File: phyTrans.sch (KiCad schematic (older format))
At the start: 2 parts

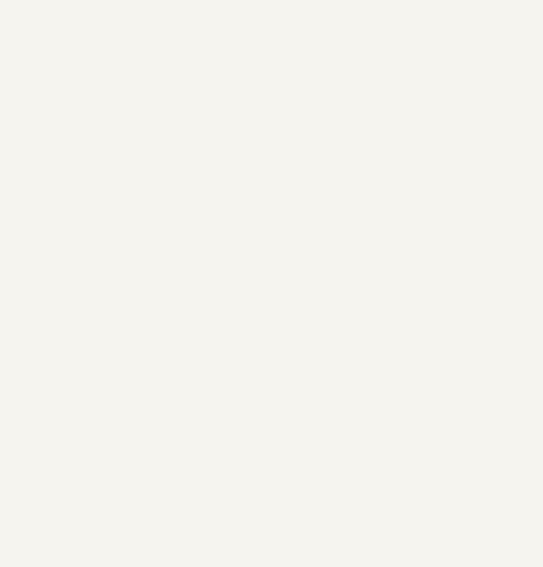
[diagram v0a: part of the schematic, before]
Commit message: Added user fields to library components.
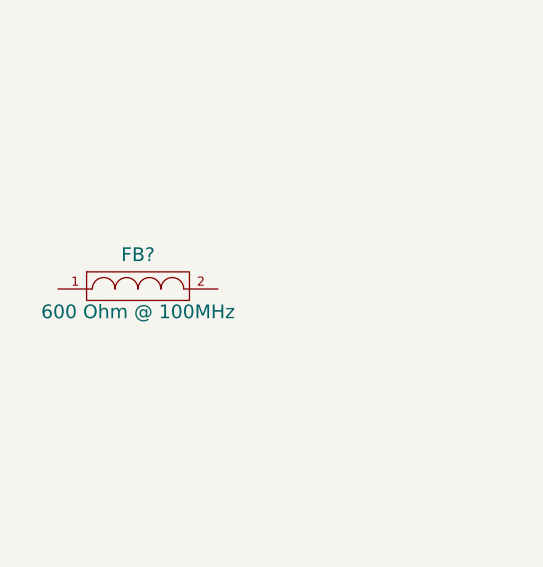
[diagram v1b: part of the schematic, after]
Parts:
- added FB?: 600 Ohm @ 100MHz, symbol FILTER
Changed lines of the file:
@@
-EESchema Schematic File Version 2  date 9/16/2011 7:37:49 PM
+EESchema Schematic File Version 2  date 9/16/2011 8:27:00 PM
 LIBS:power
 LIBS:device
@@
 $EndDescr
 $Comp
+L FILTER FB?
+U 1 1 4E73F4B4
+P 1950 2050
+F 0 "FB?" H 1950 2200 60  0000 C CNN
+F 1 "600 Ohm @ 100MHz" H 1950 1950 60  0000 C CNN
+F 4 "Digi-Key" H 1950 2050 60  0001 C CNN "Supplier"
+F 5 "P10189CT-ND" H 1950 2050 60  0001 C CNN "PN"
+F 6 "http://search.digikey.com/scripts/DkSearch/dksus.dll?Detail&name=P10189CT-ND" H 1950 2050 60  0001 C CNN "Link"
+	1    1950 2050
+	1    0    0    -1
+$EndComp
+$Comp
 L GND #PWR?

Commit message: Added power filtering to phy ckt.
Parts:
- added C? (x3): 0.1uF, symbol C
- added C? (x3): 22uF, symbol C
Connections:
- net labels removed: +1.2V
- wire segments 4 -> 15
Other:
- moved on the sheet: FB?
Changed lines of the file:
@@
-EESchema Schematic File Version 2  date 9/16/2011 8:27:00 PM
+EESchema Schematic File Version 2  date 9/16/2011 11:02:28 PM
 LIBS:power
 LIBS:device
@@
 Comment4 ""
 $EndDescr
+Wire Wire Line
+	5450 2650 5450 2750
+Wire Wire Line
+	5650 2400 5650 2750
+Wire Wire Line
+	7250 4150 7250 4050
+Wire Wire Line
+	7250 3650 6850 3650
+Connection ~ 4150 3350
+Wire Wire Line
+	3900 3350 4750 3350
+Wire Wire Line
+	4750 3250 4400 3250
+Connection ~ 4400 2850
+Wire Wire Line
+	4150 2950 4150 2850
+Wire Wire Line
+	4150 2850 4650 2850
+Wire Wire Line
+	8950 750  8950 1100
+Wire Wire Line
+	4400 3750 4150 3750
+Wire Wire Line
+	4150 3750 4150 3850
+Wire Wire Line
+	3000 3350 3200 3350
+Wire Wire Line
+	7250 4050 7000 4050
+Wire Wire Line
+	5750 2650 5750 2750
+Wire Wire Line
+	5550 2550 5550 2750
+$Comp
+L GND #PWR?
+U 1 1 4E741BA5
+P 7250 4150
+F 0 "#PWR?" H 7250 4150 30  0001 C CNN
+F 1 "GND" H 7250 4080 30  0001 C CNN
+	1    7250 4150
+	1    0    0    -1
+$EndComp
+$Comp
+L GND #PWR?
+U 1 1 4E741B4C
+P 4150 3850
+F 0 "#PWR?" H 4150 3850 30  0001 C CNN
+F 1 "GND" H 4150 3780 30  0001 C CNN
+	1    4150 3850
+	1    0    0    -1
+$EndComp
+$Comp
+L GND #PWR?
+U 1 1 4E741ADB
+P 4150 2950
+F 0 "#PWR?" H 4150 2950 30  0001 C CNN
+F 1 "GND" H 4150 2880 30  0001 C CNN
+	1    4150 2950
+	1    0    0    -1
+$EndComp
+$Comp
+L C C?
+U 1 1 4E741A67
+P 4400 3050
+F 0 "C?" H 4450 3150 50  0000 L CNN
+F 1 "22uF" H 4450 2950 50  0000 L CNN
+F 4 "Digi-Key" H 4400 3050 60  0001 C CNN "Supplier"
+F 5 "445-1422-1-ND" H 4400 3050 60  0001 C CNN "PN"
+F 6 "http://search.digikey.com/scripts/DkSearch/dksus.dll?Detail&name=445-1422-1-ND" H 4400 3050 60  0001 C CNN "Link"
+	1    4400 3050
+	1    0    0    1
+$EndComp
+$Comp
+L C C?
+U 1 1 4E741A63
+P 4150 3550
+F 0 "C?" H 4200 3650 50  0000 L CNN
+F 1 "22uF" H 4200 3450 50  0000 L CNN
+F 4 "Digi-Key" H 4150 3550 60  0001 C CNN "Supplier"
+F 5 "445-1422-1-ND" H 4150 3550 60  0001 C CNN "PN"
+F 6 "http://search.digikey.com/scripts/DkSearch/dksus.dll?Detail&name=445-1422-1-ND" H 4150 3550 60  0001 C CNN "Link"
+	1    4150 3550
+	1    0    0    -1
+$EndComp
+$Comp
+L C C?
+U 1 1 4E741495
+P 7000 3850
+F 0 "C?" H 7050 3950 50  0000 L CNN
+F 1 "22uF" H 7050 3750 50  0000 L CNN
+F 4 "Digi-Key" H 7000 3850 60  0001 C CNN "Supplier"
+F 5 "445-1422-1-ND" H 7000 3850 60  0001 C CNN "PN"
+F 6 "http://search.digikey.com/scripts/DkSearch/dksus.dll?Detail&name=445-1422-1-ND" H 7000 3850 60  0001 C CNN "Link"
+	1    7000 3850
+	1    0    0    -1
+$EndComp
+$Comp
+L C C?
+U 1 1 4E741482
+P 4650 3050
+F 0 "C?" H 4700 3150 50  0000 L CNN
+F 1 "0.1uF" H 4700 2950 50  0000 L CNN
+F 4 "Digi-Key" H 4650 3050 60  0001 C CNN "Supplier"
+F 5 "490-1673-1-ND" H 4650 3050 60  0001 C CNN "PN"
+F 6 "http://search.digikey.com/scripts/DkSearch/dksus.dll?Detail&name=490-1673-1-ND" H 4650 3050 60  0001 C CNN "Link"
+	1    4650 3050
+	1    0    0    1
+$EndComp
+$Comp
+L C C?
+U 1 1 4E741480
+P 4400 3550
+F 0 "C?" H 4450 3650 50  0000 L CNN
+F 1 "0.1uF" H 4450 3450 50  0000 L CNN
+F 4 "Digi-Key" H 4400 3550 60  0001 C CNN "Supplier"
+F 5 "490-1673-1-ND" H 4400 3550 60  0001 C CNN "PN"
+F 6 "http://search.digikey.com/scripts/DkSearch/dksus.dll?Detail&name=490-1673-1-ND" H 4400 3550 60  0001 C CNN "Link"
+	1    4400 3550
+	1    0    0    -1
+$EndComp
+$Comp
+L C C?
+U 1 1 4E740C09
+P 7250 3850
+F 0 "C?" H 7300 3950 50  0000 L CNN
+F 1 "0.1uF" H 7300 3750 50  0000 L CNN
+F 4 "Digi-Key" H 7250 3850 60  0001 C CNN "Supplier"
+F 5 "490-1673-1-ND" H 7250 3850 60  0001 C CNN "PN"
+F 6 "http://search.digikey.com/scripts/DkSearch/dksus.dll?Detail&name=490-1673-1-ND" H 7250 3850 60  0001 C CNN "Link"
+	1    7250 3850
+	1    0    0    -1
+$EndComp
 $Comp
 L FILTER FB?
 U 1 1 4E73F4B4
-P 1950 2050
-F 0 "FB?" H 1950 2200 60  0000 C CNN
-F 1 "600 Ohm @ 100MHz" H 1950 1950 60  0000 C CNN
-F 4 "Digi-Key" H 1950 2050 60  0001 C CNN "Supplier"
-F 5 "P10189CT-ND" H 1950 2050 60  0001 C CNN "PN"
-F 6 "http://search.digikey.com/scripts/DkSearch/dksus.dll?Detail&name=P10189CT-ND" H 1950 2050 60  0001 C CNN "Link"
-	1    1950 2050
+P 3550 3350
+F 0 "FB?" H 3550 3500 60  0000 C CNN
+F 1 "600 Ohm @ 100MHz" H 3550 3250 60  0000 C CNN
+F 4 "Digi-Key" H 3550 3350 60  0001 C CNN "Supplier"
+F 5 "P10189CT-ND" H 3550 3350 60  0001 C CNN "PN"
+F 6 "http://search.digikey.com/scripts/DkSearch/dksus.dll?Detail&name=P10189CT-ND" H 3550 3350 60  0001 C CNN "Link"
+	1    3550 3350
 	1    0    0    -1
 $EndComp
@@
 Text Label 8950 750  2    60   ~ 0
 LED_Signal
-Wire Wire Line
-	8950 750  8950 1100
-Wire Wire Line
-	5650 2500 5650 2750
-Wire Wire Line
-	4650 3350 4750 3350
-Wire Wire Line
-	5550 2650 5550 2750
 $Comp
 L MAGJACK RJ45_?
@@
 	-1   0    0    1
 $EndComp
-Text Label 5650 2500 2    60   ~ 0
+Text Label 5650 2400 2    60   ~ 0
 LED_Signal
 $Comp
 L GND #PWR?
 U 1 1 4E6B93CF
-P 5750 2750
-F 0 "#PWR?" H 5750 2750 30  0001 C CNN
-F 1 "GND" H 5750 2680 30  0001 C CNN
-	1    5750 2750
-	-1   0    0    1
-$EndComp
-Text Label 5550 2650 2    60   ~ 0
+P 5750 2650
+F 0 "#PWR?" H 5750 2650 30  0001 C CNN
+F 1 "GND" H 5750 2580 30  0001 C CNN
+	1    5750 2650
+	-1   0    0    1
+$EndComp
+Text Label 5550 2550 2    60   ~ 0
 RST
 $Comp
 L GND #PWR?
 U 1 1 4E6B9340
-P 5450 2750
-F 0 "#PWR?" H 5450 2750 30  0001 C CNN
-F 1 "GND" H 5450 2680 30  0001 C CNN
-	1    5450 2750
+P 5450 2650
+F 0 "#PWR?" H 5450 2650 30  0001 C CNN
+F 1 "GND" H 5450 2580 30  0001 C CNN
+	1    5450 2650
 	-1   0    0    1
 $EndComp
@@
 L +3.3V #PWR?
 U 1 1 4E6B9310
-P 4650 3350
-F 0 "#PWR?" H 4650 3310 30  0001 C CNN
-F 1 "+3.3V" H 4650 3460 30  0000 C CNN
-	1    4650 3350
-	1    0    0    -1
-$EndComp
-$Comp
-L +1.2V #PWR?
-U 1 1 4E6B92FB
-P 4750 3250
-F 0 "#PWR?" H 4750 3390 20  0001 C CNN
-F 1 "+1.2V" H 4750 3360 30  0000 C CNN
-	1    4750 3250
-	1    0    0    -1
-$EndComp
+P 3000 3350
+F 0 "#PWR?" H 3000 3310 30  0001 C CNN
+F 1 "+3.3V" H 3000 3460 30  0000 C CNN
+	1    3000 3350
+	1    0    0    -1
+$EndComp

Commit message: Labeled everything in the phy... Getting ready to setup the Heir. Schematic
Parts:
- removed RJ45_?: MAGJACK, symbol MAGJACK
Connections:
- net labels added: CRS_DV, INTRP, MDC, MDID, REF_CLK, REXT, RXD0, RXD1, RXER, RXM, RXP, TXD1, TXD2, TXEN, TXM, TXP, XD, XI
- wire segments 15 -> 32
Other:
- moved on the sheet: C?, FB?
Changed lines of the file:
@@
-EESchema Schematic File Version 2  date 9/16/2011 11:02:28 PM
+EESchema Schematic File Version 2  date 9/21/2011 8:12:33 PM
 LIBS:power
 LIBS:device
@@
 Sheet 1 1
 Title "noname.sch"
-Date "17 sep 2011"
+Date "22 sep 2011"
 Rev ""
 Comp ""
@@
 $EndDescr
 Wire Wire Line
+	7950 3650 6850 3650
+Wire Wire Line
+	5950 4900 5950 4250
+Wire Wire Line
+	5750 4700 5750 4250
+Wire Wire Line
+	4500 3750 4750 3750
+Wire Wire Line
+	4500 3550 4750 3550
+Wire Wire Line
+	7250 3550 6850 3550
+Wire Wire Line
+	6850 3350 7250 3350
+Wire Wire Line
+	7250 3450 6850 3450
+Wire Wire Line
+	5650 4250 5650 4600
+Wire Wire Line
+	4750 3450 4500 3450
+Wire Wire Line
+	5950 2200 5950 2750
+Wire Wire Line
 	5450 2650 5450 2750
 Wire Wire Line
 	5650 2400 5650 2750
 Wire Wire Line
-	7250 4150 7250 4050
-Wire Wire Line
-	7250 3650 6850 3650
-Connection ~ 4150 3350
-Wire Wire Line
-	3900 3350 4750 3350
+	7950 4150 7950 4050
+Connection ~ 3700 3350
 Wire Wire Line
 	4750 3250 4400 3250
@@
 	4150 2850 4650 2850
 Wire Wire Line
-	8950 750  8950 1100
-Wire Wire Line
-	4400 3750 4150 3750
-Wire Wire Line
-	4150 3750 4150 3850
-Wire Wire Line
-	3000 3350 3200 3350
-Wire Wire Line
-	7250 4050 7000 4050
+	3950 3750 3700 3750
+Wire Wire Line
+	3700 3750 3700 3850
+Wire Wire Line
+	2550 3350 2750 3350
+Wire Wire Line
+	7950 4050 7700 4050
 Wire Wire Line
 	5750 2650 5750 2750
 Wire Wire Line
 	5550 2550 5550 2750
+Wire Wire Line
+	5850 2300 5850 2750
+Wire Wire Line
+	6050 2050 6050 2750
+Wire Wire Line
+	5550 4250 5550 4500
+Wire Wire Line
+	6850 3250 7250 3250
+Wire Wire Line
+	7250 3750 6850 3750
+Wire Wire Line
+	4500 3650 4750 3650
+Wire Wire Line
+	4750 3350 3450 3350
+Wire Wire Line
+	5850 4800 5850 4250
+Wire Wire Line
+	6050 5000 6050 4250
+Text Label 7250 3250 2    60   ~ 0
+INTRP
+Text Label 7250 3350 2    60   ~ 0
+RXER
+Text Label 7250 3450 2    60   ~ 0
+REF_CLK
+Text Label 7250 3550 2    60   ~ 0
+CRS_DV
+Text Label 7250 3750 2    60   ~ 0
+RXD0
+Text Label 6050 5000 2    60   ~ 0
+RXD1
+Text Label 5950 4900 2    60   ~ 0
+MDC
+Text Label 5850 4800 2    60   ~ 0
+MDID
+Text Label 5750 4700 2    60   ~ 0
+REXT
+Text Label 5650 4600 2    60   ~ 0
+XI
+Text Label 5550 4500 2    60   ~ 0
+XD
+Text Label 4500 3750 0    60   ~ 0
+TXP
+Text Label 4500 3650 0    60   ~ 0
+TXM
+Text Label 4500 3550 0    60   ~ 0
+RXP
+Text Label 4500 3450 0    60   ~ 0
+RXM
+Text Label 4500 3450 0    60   ~ 0
+RXM
+Text Label 6050 2050 2    60   ~ 0
+TXEN
+Text Label 5950 2200 2    60   ~ 0
+TXD2
+Text Label 5850 2300 2    60   ~ 0
+TXD1
 $Comp
 L GND #PWR?
 U 1 1 4E741BA5
-P 7250 4150
-F 0 "#PWR?" H 7250 4150 30  0001 C CNN
-F 1 "GND" H 7250 4080 30  0001 C CNN
-	1    7250 4150
+P 7950 4150
+F 0 "#PWR?" H 7950 4150 30  0001 C CNN
+F 1 "GND" H 7950 4080 30  0001 C CNN
+	1    7950 4150
 	1    0    0    -1
 $EndComp
@@
 L GND #PWR?
 U 1 1 4E741B4C
-P 4150 3850
-F 0 "#PWR?" H 4150 3850 30  0001 C CNN
-F 1 "GND" H 4150 3780 30  0001 C CNN
-	1    4150 3850
+P 3700 3850
+F 0 "#PWR?" H 3700 3850 30  0001 C CNN
+F 1 "GND" H 3700 3780 30  0001 C CNN
+	1    3700 3850
 	1    0    0    -1
 $EndComp
@@
 L C C?
 U 1 1 4E741A63
-P 4150 3550
-F 0 "C?" H 4200 3650 50  0000 L CNN
-F 1 "22uF" H 4200 3450 50  0000 L CNN
-F 4 "Digi-Key" H 4150 3550 60  0001 C CNN "Supplier"
-F 5 "445-1422-1-ND" H 4150 3550 60  0001 C CNN "PN"
-F 6 "http://search.digikey.com/scripts/DkSearch/dksus.dll?Detail&name=445-1422-1-ND" H 4150 3550 60  0001 C CNN "Link"
-	1    4150 3550
+P 3700 3550
+F 0 "C?" H 3750 3650 50  0000 L CNN
+F 1 "22uF" H 3750 3450 50  0000 L CNN
+F 4 "Digi-Key" H 3700 3550 60  0001 C CNN "Supplier"
+F 5 "445-1422-1-ND" H 3700 3550 60  0001 C CNN "PN"
+F 6 "http://search.digikey.com/scripts/DkSearch/dksus.dll?Detail&name=445-1422-1-ND" H 3700 3550 60  0001 C CNN "Link"
+	1    3700 3550
 	1    0    0    -1
 $EndComp
@@
 L C C?
 U 1 1 4E741495
-P 7000 3850
-F 0 "C?" H 7050 3950 50  0000 L CNN
-F 1 "22uF" H 7050 3750 50  0000 L CNN
-F 4 "Digi-Key" H 7000 3850 60  0001 C CNN "Supplier"
-F 5 "445-1422-1-ND" H 7000 3850 60  0001 C CNN "PN"
-F 6 "http://search.digikey.com/scripts/DkSearch/dksus.dll?Detail&name=445-1422-1-ND" H 7000 3850 60  0001 C CNN "Link"
-	1    7000 3850
+P 7700 3850
+F 0 "C?" H 7750 3950 50  0000 L CNN
+F 1 "22uF" H 7750 3750 50  0000 L CNN
+F 4 "Digi-Key" H 7700 3850 60  0001 C CNN "Supplier"
+F 5 "445-1422-1-ND" H 7700 3850 60  0001 C CNN "PN"
+F 6 "http://search.digikey.com/scripts/DkSearch/dksus.dll?Detail&name=445-1422-1-ND" H 7700 3850 60  0001 C CNN "Link"
+	1    7700 3850
 	1    0    0    -1
 $EndComp
@@
 L C C?
 U 1 1 4E741480
-P 4400 3550
-F 0 "C?" H 4450 3650 50  0000 L CNN
-F 1 "0.1uF" H 4450 3450 50  0000 L CNN
-F 4 "Digi-Key" H 4400 3550 60  0001 C CNN "Supplier"
-F 5 "490-1673-1-ND" H 4400 3550 60  0001 C CNN "PN"
-F 6 "http://search.digikey.com/scripts/DkSearch/dksus.dll?Detail&name=490-1673-1-ND" H 4400 3550 60  0001 C CNN "Link"
-	1    4400 3550
+P 3950 3550
+F 0 "C?" H 4000 3650 50  0000 L CNN
+F 1 "0.1uF" H 4000 3450 50  0000 L CNN
+F 4 "Digi-Key" H 3950 3550 60  0001 C CNN "Supplier"
+F 5 "490-1673-1-ND" H 3950 3550 60  0001 C CNN "PN"
+F 6 "http://search.digikey.com/scripts/DkSearch/dksus.dll?Detail&name=490-1673-1-ND" H 3950 3550 60  0001 C CNN "Link"
+	1    3950 3550
 	1    0    0    -1
 $EndComp
@@
 L C C?
 U 1 1 4E740C09
-P 7250 3850
-F 0 "C?" H 7300 3950 50  0000 L CNN
-F 1 "0.1uF" H 7300 3750 50  0000 L CNN
-F 4 "Digi-Key" H 7250 3850 60  0001 C CNN "Supplier"
-F 5 "490-1673-1-ND" H 7250 3850 60  0001 C CNN "PN"
-F 6 "http://search.digikey.com/scripts/DkSearch/dksus.dll?Detail&name=490-1673-1-ND" H 7250 3850 60  0001 C CNN "Link"
-	1    7250 3850
+P 7950 3850
+F 0 "C?" H 8000 3950 50  0000 L CNN
+F 1 "0.1uF" H 8000 3750 50  0000 L CNN
+F 4 "Digi-Key" H 7950 3850 60  0001 C CNN "Supplier"
+F 5 "490-1673-1-ND" H 7950 3850 60  0001 C CNN "PN"
+F 6 "http://search.digikey.com/scripts/DkSearch/dksus.dll?Detail&name=490-1673-1-ND" H 7950 3850 60  0001 C CNN "Link"
+	1    7950 3850
 	1    0    0    -1
 $EndComp
@@
 L FILTER FB?
 U 1 1 4E73F4B4
-P 3550 3350
-F 0 "FB?" H 3550 3500 60  0000 C CNN
-F 1 "600 Ohm @ 100MHz" H 3550 3250 60  0000 C CNN
-F 4 "Digi-Key" H 3550 3350 60  0001 C CNN "Supplier"
-F 5 "P10189CT-ND" H 3550 3350 60  0001 C CNN "PN"
-F 6 "http://search.digikey.com/scripts/DkSearch/dksus.dll?Detail&name=P10189CT-ND" H 3550 3350 60  0001 C CNN "Link"
-	1    3550 3350
-	1    0    0    -1
-$EndComp
-$Comp
-L GND #PWR?
-U 1 1 4E6EC4DB
-P 8850 1100
-F 0 "#PWR?" H 8850 1100 30  0001 C CNN
-F 1 "GND" H 8850 1030 30  0001 C CNN
-	1    8850 1100
-	-1   0    0    1
-$EndComp
-Text Label 8950 750  2    60   ~ 0
-LED_Signal
-$Comp
-L MAGJACK RJ45_?
-U 1 1 4E6EC1A4
-P 8600 1600
-F 0 "RJ45_?" H 8600 2000 60  0000 C CNN
-F 1 "MAGJACK" H 8600 2100 60  0000 C CNN
-	1    8600 1600
-	-1   0    0    1
+P 3100 3350
+F 0 "FB?" H 3100 3500 60  0000 C CNN
+F 1 "600 Ohm @ 100MHz" H 3100 3250 60  0000 C CNN
+F 4 "Digi-Key" H 3100 3350 60  0001 C CNN "Supplier"
+F 5 "P10189CT-ND" H 3100 3350 60  0001 C CNN "PN"
+F 6 "http://search.digikey.com/scripts/DkSearch/dksus.dll?Detail&name=P10189CT-ND" H 3100 3350 60  0001 C CNN "Link"
+	1    3100 3350
+	1    0    0    -1
 $EndComp
 Text Label 5650 2400 2    60   ~ 0
@@
 L +3.3V #PWR?
 U 1 1 4E6B9310
-P 3000 3350
-F 0 "#PWR?" H 3000 3310 30  0001 C CNN
-F 1 "+3.3V" H 3000 3460 30  0000 C CNN
-	1    3000 3350
-	1    0    0    -1
-$EndComp
+P 2550 3350
+F 0 "#PWR?" H 2550 3310 30  0001 C CNN
+F 1 "+3.3V" H 2550 3460 30  0000 C CNN
+	1    2550 3350
+	1    0    0    -1
+$EndComp
